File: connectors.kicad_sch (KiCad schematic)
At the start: 0 parts

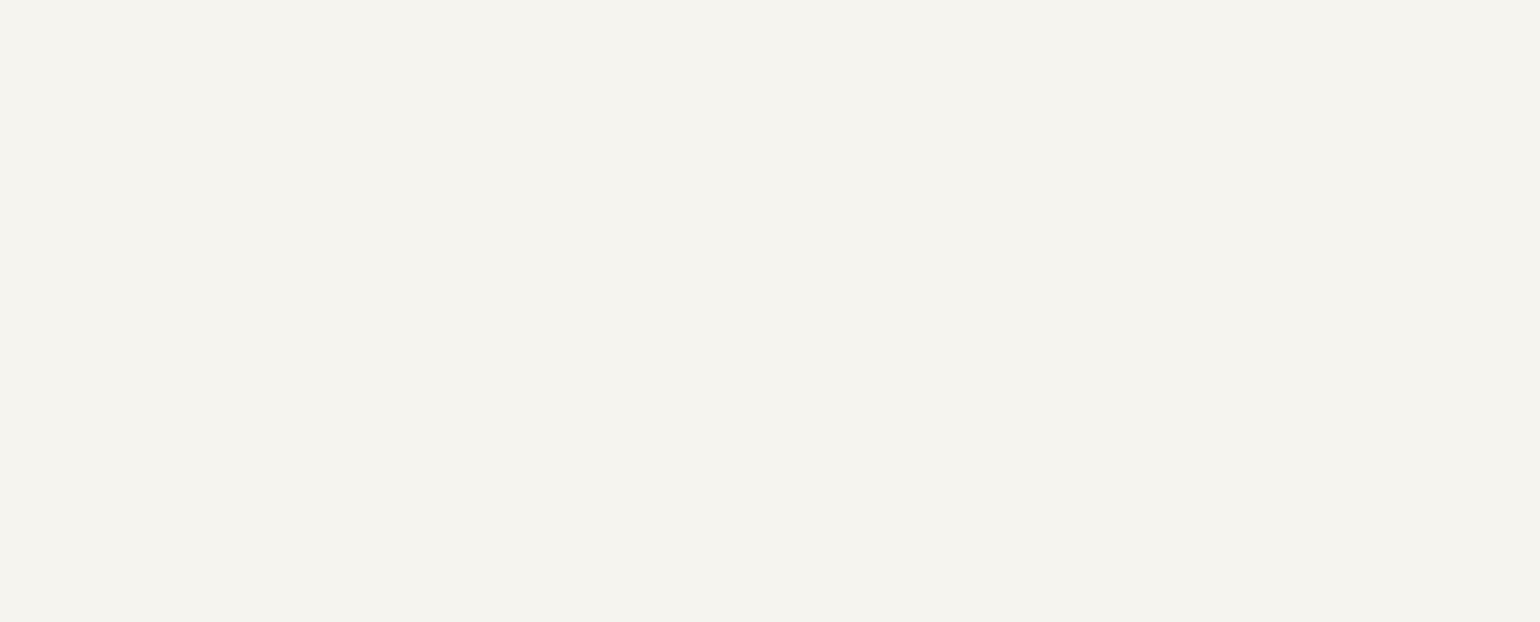
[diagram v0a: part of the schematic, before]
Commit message: SCH:[Connectors]: Added connectors and lables.
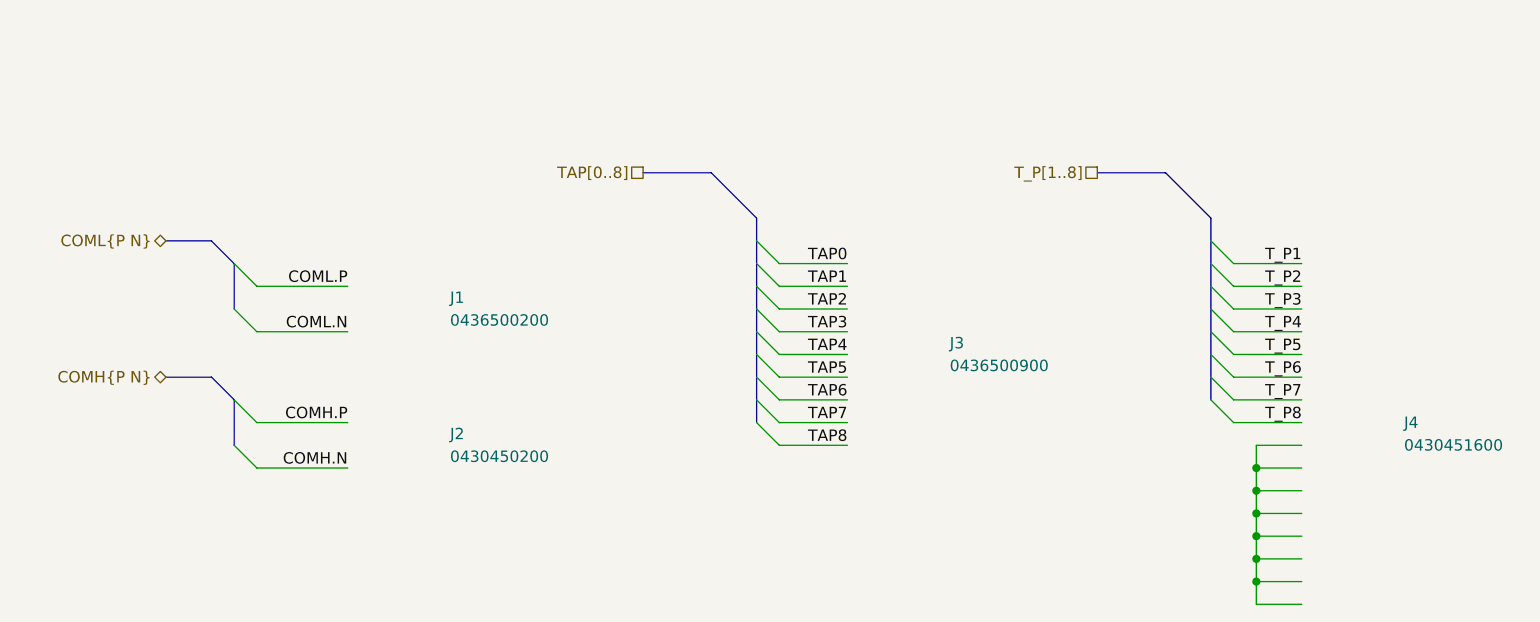
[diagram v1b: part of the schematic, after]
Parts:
- added J1: 0436500200, remote_0436500200:CONN_SD-43650-001_02_MOL, symbol remote_0436500200:0436500200
- added J2: 0430450200, remote_0430450200:CONN_SD-43045-001_02_MOL, symbol remote_0430450200:0430450200
- added J3: 0436500900, remote_0436500900:CONN_SD-43650-001_09_MOL, symbol remote_0436500900:0436500900
- added J4: 0430451600, remote_0430451600:CONN_SD-43045-001_16_MOL, symbol remote_0430451600:0430451600
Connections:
- new net: J4.10, J4.11, J4.12, J4.13, J4.14, J4.15, J4.16, J4.9
- new net COMH.N: J2.2
- new net COMH.P: J2.1
- new net COML.N: J1.2
- new net COML.P: J1.1
- new net TAP0: J3.1
- new net TAP1: J3.2
- new net TAP2: J3.3
- new net TAP3: J3.4
- new net TAP4: J3.5
- new net TAP5: J3.6
- new net TAP6: J3.7
- new net TAP7: J3.8
- new net TAP8: J3.9
- new net T_P1: J4.1
- new net T_P2: J4.2
- new net T_P3: J4.3
- new net T_P4: J4.4
- new net T_P5: J4.5
- new net T_P6: J4.6
- new net T_P7: J4.7
- new net T_P8: J4.8

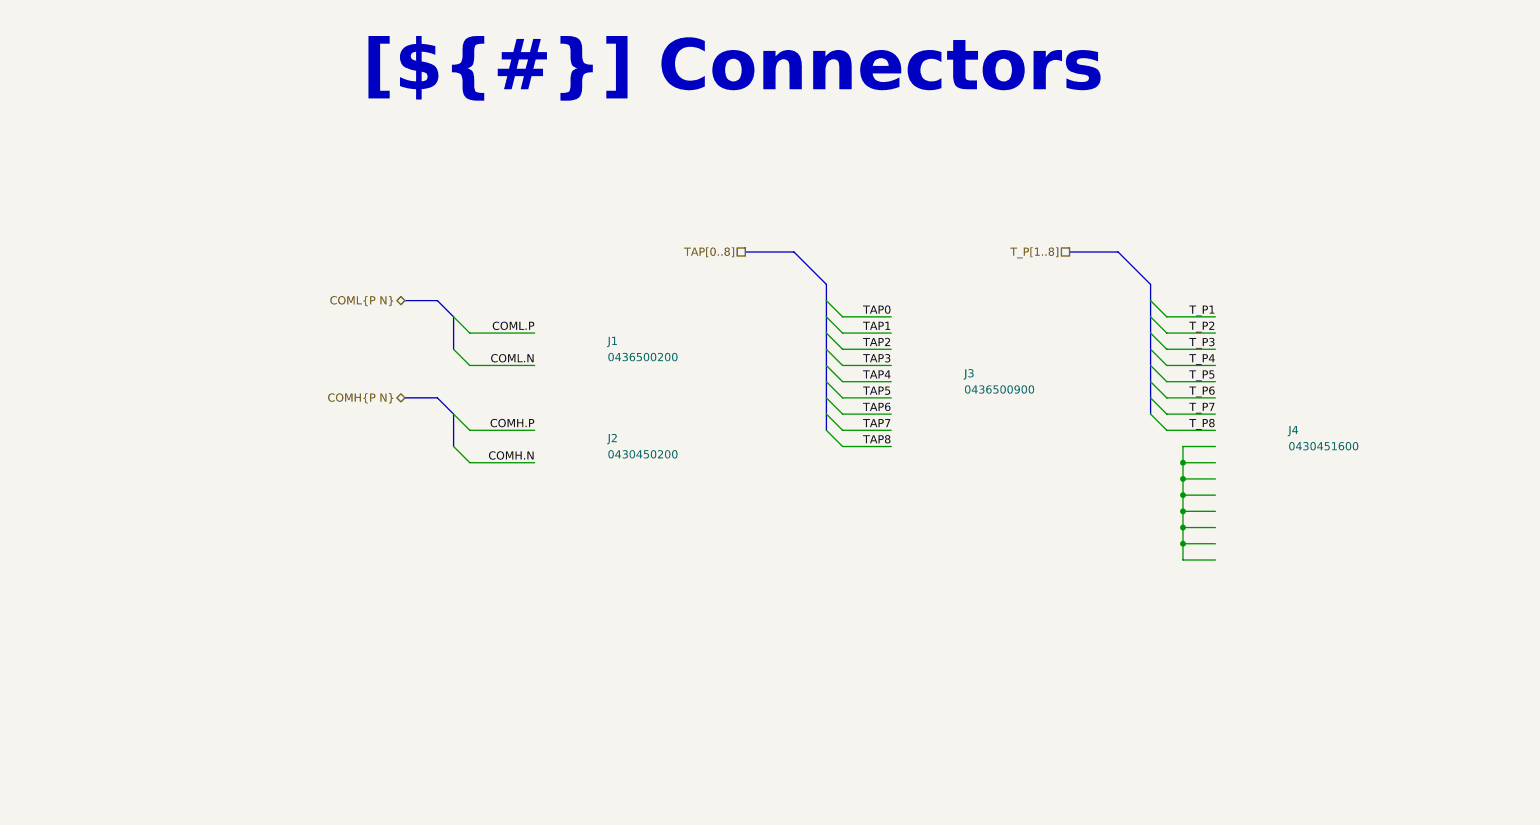
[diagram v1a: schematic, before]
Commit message: SCH: Schmatic is close to final, need to resolve a few ERC errors nothing major. Largest change will be adding seporate wires for VBAT and RefGround / Tap 0. connector position and types may change as mechaincal posision/layout is finalaized as well so holding off on layout for now.
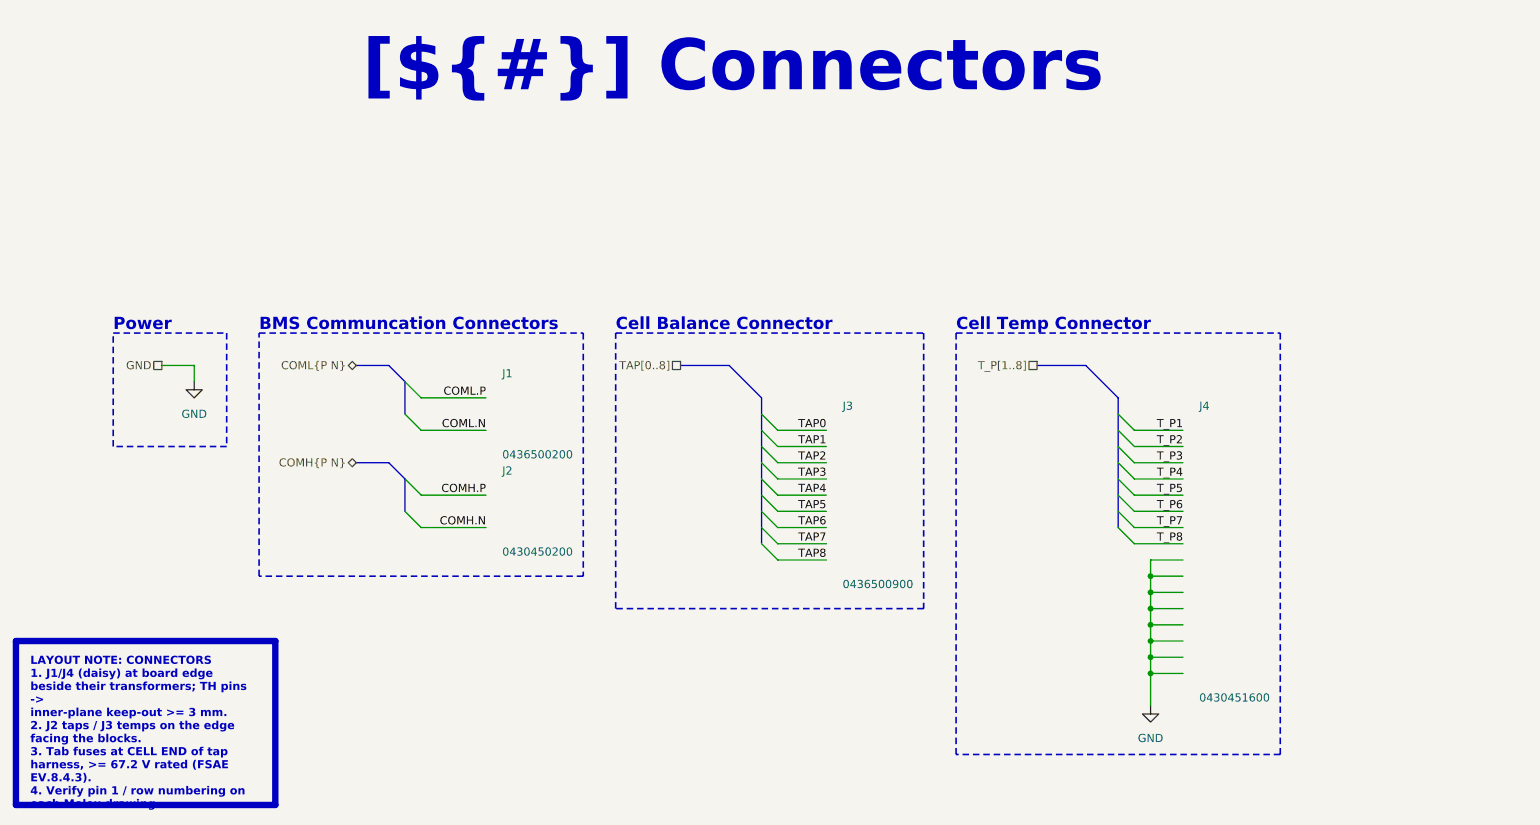
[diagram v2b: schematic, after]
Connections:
- net GND: now reaches J4.10, J4.11, J4.12, J4.13, J4.14, J4.15, J4.16, J4.9
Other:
- note added: "BMS Communcation Connectors"
- note added: "Cell Balance Connector"
- note added: "Cell Temp Connector"
- note added: "Power"

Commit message: SCH[Cleaning]:Updated Connectors not sure still, added sprate bat and ground connections, updated commincation conncetors. PCB[Layout]:Inital layout of compents need to fit on board size once tap connecton method is decided.
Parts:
- removed J1: 0436500200, remote_0436500200:CONN_SD-43650-001_02_MOL, symbol remote_0436500200:0436500200
- removed J2: 0430450200, remote_0430450200:CONN_SD-43045-001_02_MOL, symbol remote_0430450200:0430450200
- removed J3: 0436500900, remote_0436500900:CONN_SD-43650-001_09_MOL, symbol remote_0436500900:0436500900
- removed J4: 0430451600, remote_0430451600:CONN_SD-43045-001_16_MOL, symbol remote_0430451600:0430451600
- added J1: 0436500218, remote_0436500218:CONN_SD-43650-007_02_MOL, symbol remote_0436500218:0436500218
- added J2: 0430450212, remote_0430450212:CONN_SD-43045-005_02_MOL, symbol remote_0430450212:0430450212
- added J3: 0430451612, remote_0430451612:CONN_SD-43045-005_16_MOL, symbol remote_0430451612:0430451612
- added J4: 0436501200, remote_0436501200:CONN_SD-43650-001_12_MOL, symbol remote_0430451200:0430451200
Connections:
- net COMH.N: now also J2.2
- net COMH.P: now also J2.1
- net COML.N: now also J1.1
- net COML.P: now also J1.2
- net GND: now also J3.10, J3.11, J3.12, J3.13, J3.14, J3.15, J3.16, J3.9, J4.12
- net TAP0: now also J4.11
- net TAP1: now also J4.10
- net TAP2: now also J4.9
- net TAP3: now also J4.8
- net TAP4: now also J4.7
- net TAP5: now also J4.6
- net TAP6: now also J4.5
- net TAP7: now also J4.4
- net TAP8: now also J4.3
- net T_P1: now also J3.8
- net T_P2: now also J3.7
- net T_P3: now also J3.6
- net T_P4: now also J3.5
- net T_P5: now also J3.4
- net T_P6: now also J3.3
- net T_P7: now also J3.2
- net T_P8: now also J3.1
- new net VMODULE: J4.1
- no-connect marks 0 -> 1

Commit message: PCB[Part Layout]: Working on routing and part arragement more, thinking im going to go with the two row connector for bat connections, might have to put parts on both sides for cleaner routing for bal/sens filter caps. 0603 so wouldnt be too bad to solder.
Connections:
- net COML.N: now also J1.2; no longer J1.1
- net COML.P: now also J1.1; no longer J1.2
- net GND: now also J4.1; no longer J4.12
- net TAP0: now also J4.2; no longer J4.11
- net TAP1: now also J4.3; no longer J4.10
- net TAP2: now also J4.4; no longer J4.9
- net TAP3: now also J4.5; no longer J4.8
- net TAP4: now also J4.6; no longer J4.7
- net TAP5: now also J4.7; no longer J4.6
- net TAP6: now also J4.8; no longer J4.5
- net TAP7: now also J4.9; no longer J4.4
- net TAP8: now also J4.10; no longer J4.3
- net VMODULE: now also J4.12; no longer J4.1

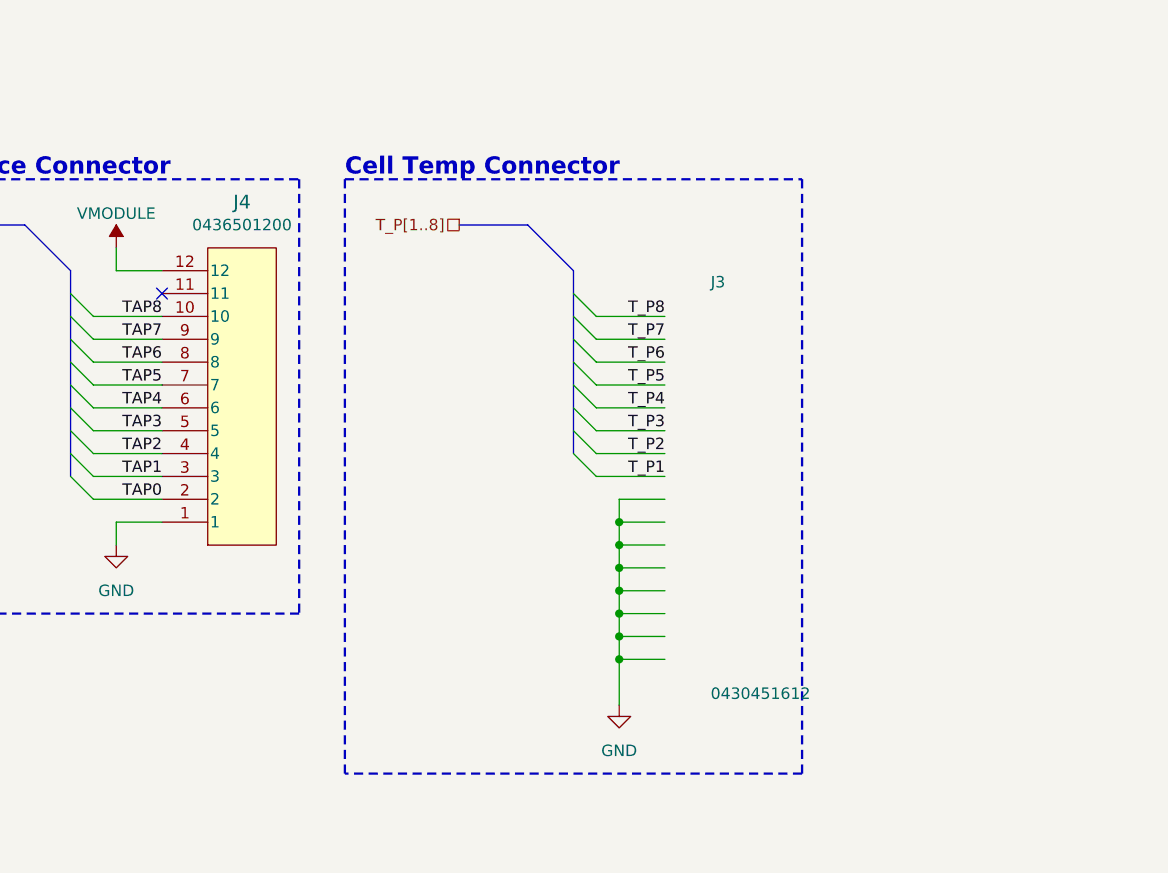
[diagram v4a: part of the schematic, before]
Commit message: SCH[Connector]: Updated tap, and temp connectors to two row variants for space, combined grounds to one pin for the temp assuming the battery interface board combines those grounds.
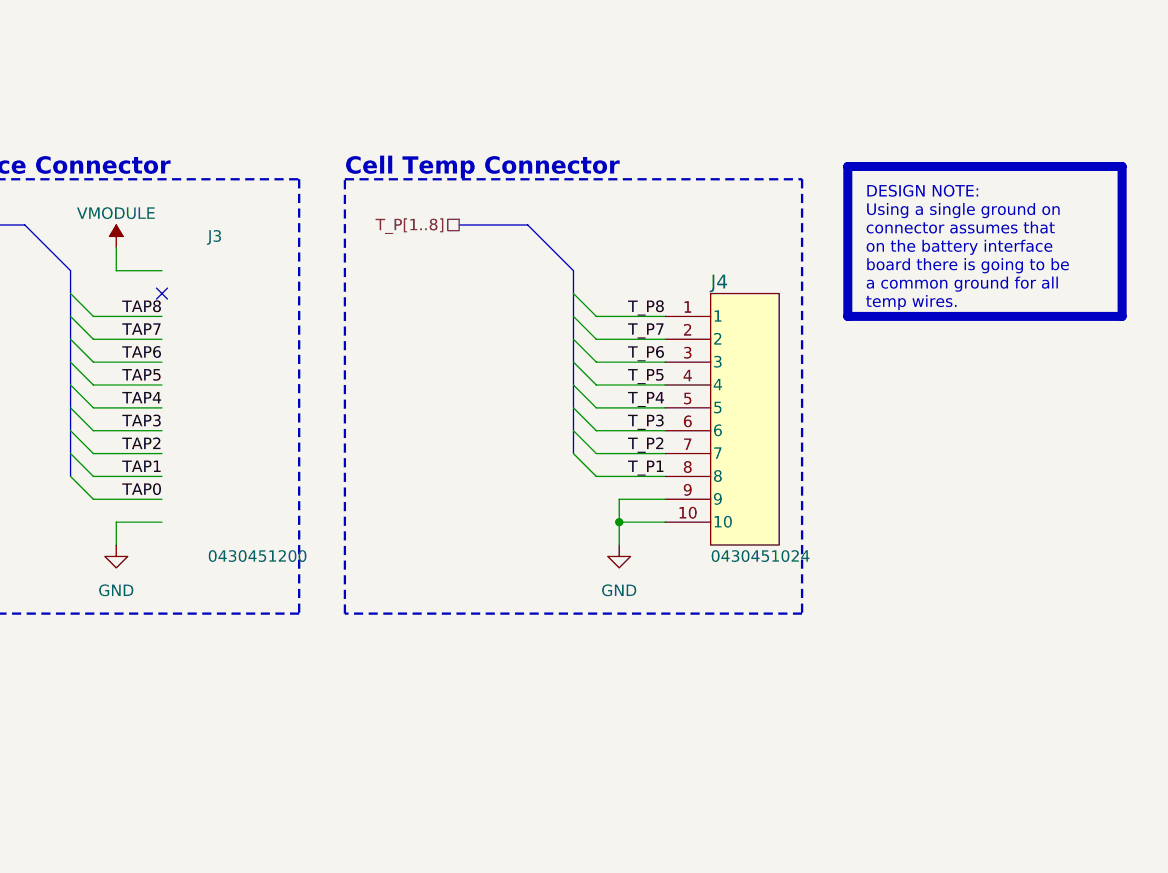
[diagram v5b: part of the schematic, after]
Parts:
- removed J3: 0430451612, remote_0430451612:CONN_SD-43045-005_16_MOL, symbol remote_0430451612:0430451612
- removed J4: 0436501200, remote_0436501200:CONN_SD-43650-001_12_MOL, symbol remote_0430451200:0430451200
- added J3: 0430451200, remote_0430451200:CONN_SD-43045-001_12_MOL, symbol remote_0430451200:0430451200
- added J4: 0430451024, remote_0430451024:CONN_SD-43045-009_10_MOL, symbol remote_0430451024:0430451024
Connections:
- net GND: now also J3.12, J4.10, J4.9
- net TAP0: now also J3.11
- net TAP1: now also J3.10
- net TAP2: now also J3.9
- net TAP3: now also J3.8
- net TAP4: now also J3.7
- net TAP5: now also J3.6
- net TAP6: now also J3.5
- net TAP7: now also J3.4
- net TAP8: now also J3.3
- net T_P1: now also J4.8
- net T_P2: now also J4.7
- net T_P3: now also J4.6
- net T_P4: now also J4.5
- net T_P5: now also J4.4
- net T_P6: now also J4.3
- net T_P7: now also J4.2
- net T_P8: now also J4.1
- net VMODULE: now also J3.1
